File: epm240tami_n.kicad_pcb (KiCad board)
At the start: 2 copper layers, 63.5 x 41.9 mm, 25 parts, among them CON1 BARREL_JACK, P1 CONN_01X03, P2 CONN_01X02, P3 CONN_01X03, P4 CONN_02X22, P5 CONN_02X22, P6 JTAG, P7 CONN_01X07, U1 EPM240T100C5N, U2 NCP1117ST33T3G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

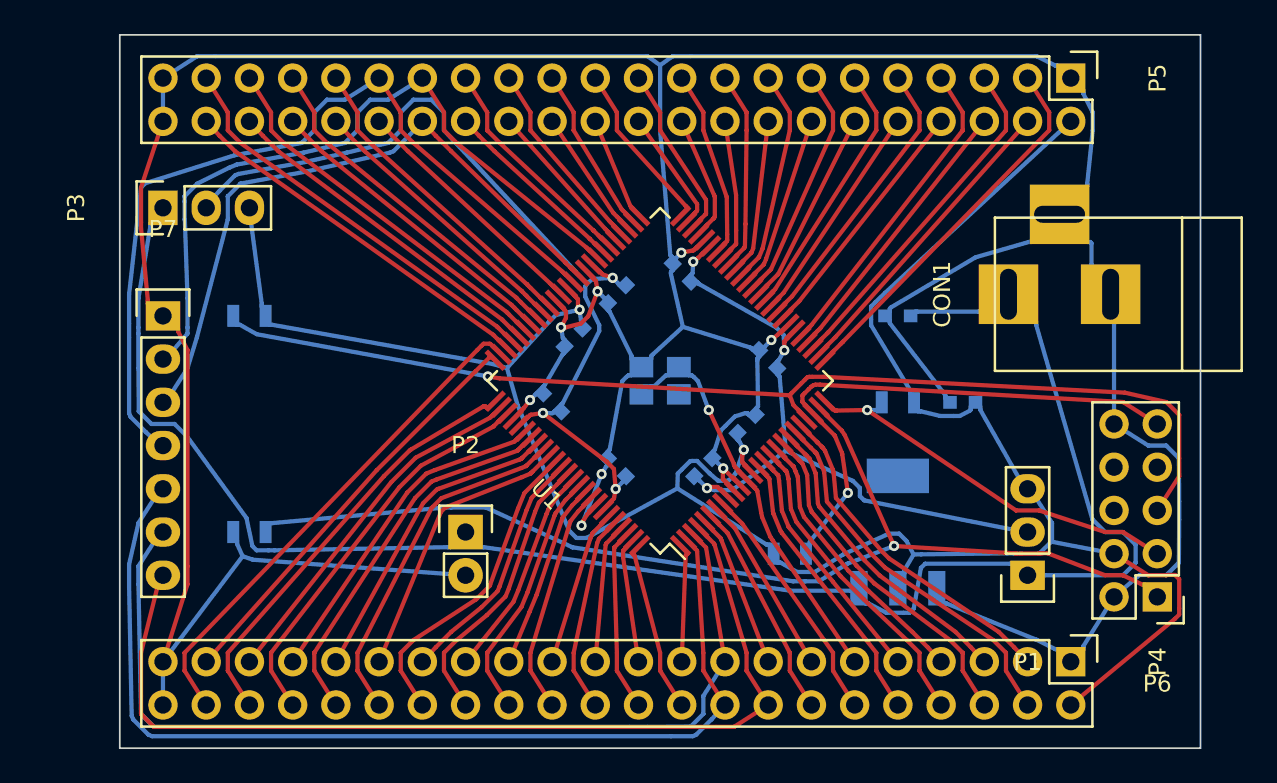
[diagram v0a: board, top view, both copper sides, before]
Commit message: Updated schematic and moved DI/DO around to reduce routing due to new placement. Added PDF file
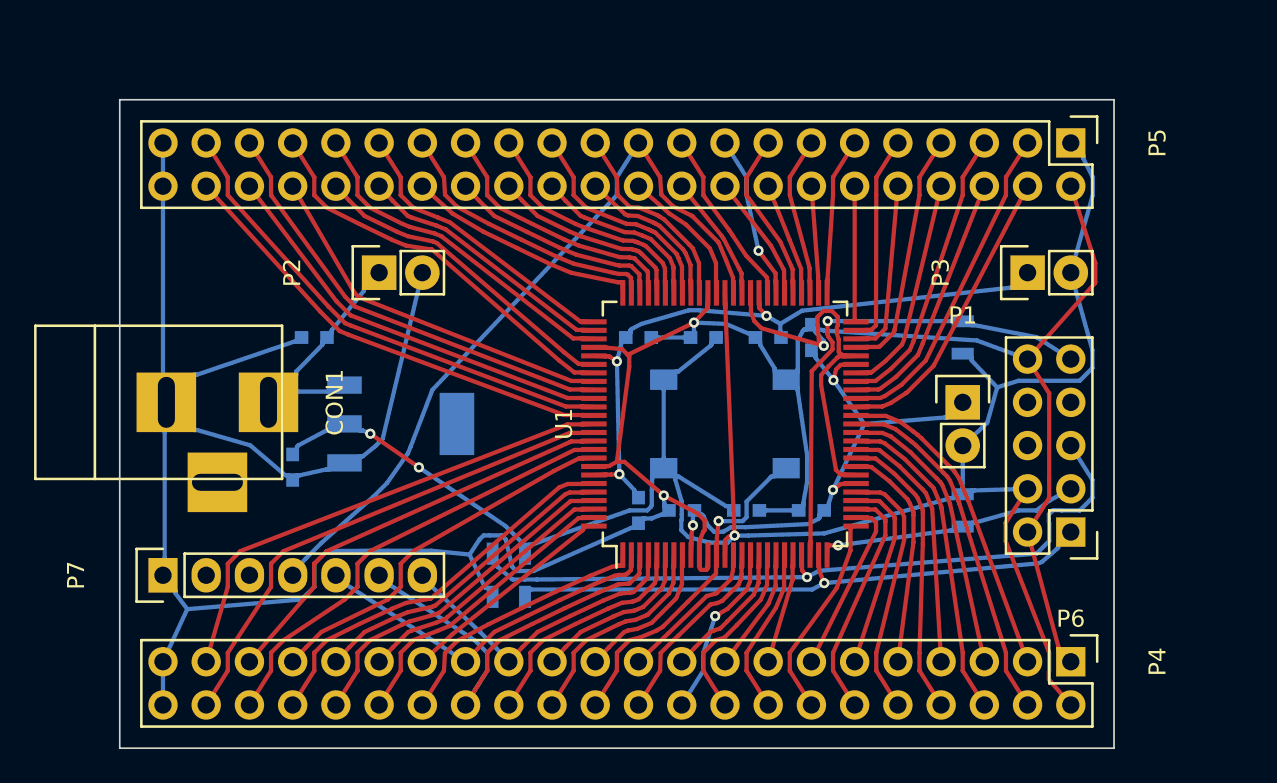
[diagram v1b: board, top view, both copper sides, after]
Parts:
- CON1: value BARREL_JACK -> AB2_POWER_BARREL
- P1, P3: value CONN_01X03 -> CONN_01X02; footprint Pin_Headers:Pin_Header_Straight_1x03 -> Pin_Headers:Pin_Header_Straight_1x02
- U2: value NCP1117ST33T3G -> AMS1117-3.3V
- X1: footprint Crystals_Oscillators_SMD:crystal_FA238-TSX3225 -> Crystals_Oscillators_SMD:crystal_HXO-3
- moved CON1 56.2 mm to (128.3, 63.5), turned to 0 degrees
- moved P3 50.9 mm to (179.1, 55.9)
- moved C2 39.6 mm to (135.9, 67.3), turned to 270 degrees
- moved C1 34.3 mm to (137.2, 59.7)
- moved U2 29.9 mm to (142.2, 64.8), turned to 90 degrees
- moved R3 20.7 mm to (148.6, 72.4)
- moved R2 16.3 mm to (175.3, 59.7), turned to 90 degrees
- moved P2 16.1 mm to (141.0, 55.9), turned to 90 degrees
- moved C7 15.9 mm to (166.4, 69.8), turned to 180 degrees
- moved R1 15.7 mm to (148.6, 74.9)
- moved P7 15.2 mm to (128.3, 73.7), turned to 90 degrees
- moved P1 10.9 mm to (175.3, 63.5), turned to 0 degrees
- moved C9 9.25 mm to (163.8, 59.7), turned to 180 degrees
- moved C4 7.62 mm to (160.0, 59.7), turned to 180 degrees
- moved R4 7.41 mm to (175.3, 69.8), turned to 270 degrees
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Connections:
- CON1 pad 3: GND -> (no net)
- P1 pad 1: VCC -> /VCCIO1
- P1 pad 2: /VCCIO1 -> +3V3
- P3 pad 1: VCC -> /VCCIO2
- P3 pad 2: /VCCIO2 -> +3V3
- P4 pad 10: /IO14 -> /IO30
- P4 pad 11: /CLK_CORE -> /IO29
- P4 pad 12: /IO8 -> /IO28
- P4 pad 13: /IO7 -> /IO27
- P4 pad 14: /IO6 -> /IO26
- P4 pad 15: /IO5 -> /IO21
- P4 pad 16: /DP2 -> /IO20
- P4 pad 17: /DP1 -> /IO19
- P4 pad 18: /DM -> /IO18
- P4 pad 19: /IO1 -> /IO17
- P4 pad 20: /IO100 -> /IO16
- P4 pad 21: /IO99 -> /IO14
- P4 pad 22: /IO98 -> /IO15
- P4 pad 23: /IO97 -> /IO8
- P4 pad 24: /IO96 -> /CLK_CORE
- P4 pad 25: /IO95 -> /IO6
- P4 pad 26: /IO92 -> /IO7
- P4 pad 27: /IO91 -> /DP2
- P4 pad 28: /IO90 -> /IO5
- P4 pad 29: /IO89 -> /DM
- P4 pad 3: /IO21 -> /IO39
- P4 pad 30: /IO88 -> /DP1
- P4 pad 31: /IO87 -> /IO100
- P4 pad 32: /IO86 -> /IO1
- P4 pad 33: /IO85 -> /IO98
- P4 pad 34: /IO84 -> /IO99
- P4 pad 35: /IO83 -> /IO96
- P4 pad 36: /IO82 -> /IO97
- P4 pad 37: /IO81 -> /IO92
- P4 pad 38: /IO78 -> /IO95
- P4 pad 39: /IO77 -> /IO90
- P4 pad 4: /IO20 -> /IO38
- P4 pad 40: /IO76 -> /IO91
- P4 pad 41: /IO75 -> /DI
- P4 pad 42: /IO74 -> /DO
- P4 pad 5: /IO19 -> /IO37
- P4 pad 6: /IO18 -> /IO36
- P4 pad 7: /IO17 -> /IO35
- P4 pad 8: /IO16 -> /IO34
- P4 pad 9: /IO15 -> /IO33
- P5 pad 1: GND -> +3V3
- P5 pad 10: /IO35 -> /IO48
- P5 pad 11: /IO36 -> /IO51
- P5 pad 12: /IO37 -> /IO50
- P5 pad 13: /IO38 -> /IO53
- P5 pad 14: /IO39 -> /IO52
- P5 pad 15: /IO40 -> /IO55
- P5 pad 16: /IO41 -> /IO54
- P5 pad 17: /IO42 -> /IO57
- P5 pad 18: /IO43 -> /IO56
- P5 pad 19: /IO44 -> /IO58
- P5 pad 2: +3V3 -> GND
- P5 pad 20: /IO47 -> /IO61
- P5 pad 21: /IO48 -> /IO62
- P5 pad 22: /IO49 -> /IO64
- P5 pad 23: /IO50 -> /IO66
- P5 pad 24: /IO51 -> /IO67
- P5 pad 25: /IO52 -> /IO68
- P5 pad 26: /IO53 -> /IO69
- P5 pad 27: /IO54 -> /IO70
- P5 pad 28: /IO55 -> /IO71
- P5 pad 29: /IO56 -> /IO72
- P5 pad 3: /IO26 -> /IO41
- P5 pad 30: /IO57 -> /IO73
- P5 pad 31: /DI -> /IO74
- P5 pad 32: /DO -> /IO75
- P5 pad 33: /IO62 -> /IO76
- P5 pad 34: /IO64 -> /IO77
- P5 pad 35: /IO66 -> /IO78
- P5 pad 36: /IO67 -> /IO81
- P5 pad 37: /IO68 -> /IO82
- P5 pad 38: /IO69 -> /IO83
- P5 pad 39: /IO70 -> /IO84
- P5 pad 4: /IO27 -> /IO40
- P5 pad 40: /IO71 -> /IO85
- P5 pad 41: /IO72 -> /IO86
- P5 pad 42: /IO73 -> /IO87
- P5 pad 5: /IO28 -> /IO43
- P5 pad 6: /IO29 -> /IO42
- P5 pad 7: /IO30 -> /IO47
- P5 pad 8: /IO33 -> /IO44
- P5 pad 9: /IO34 -> /IO49
- U1 pad 58: /DI -> /IO58
- U1 pad 61: /DO -> /IO61
- U1 pad 88: /IO88 -> /DI
- U1 pad 89: /IO89 -> /DO
- X1 pad 1: (no net) -> +3V3
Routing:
- net VCC: track 104.5 -> 14.9 mm
- net /DP2: track 57.4 -> 18.3 mm
- net /DM: track 60.4 -> 21.4 mm
- net GND: track 257.1 -> 224.3 mm, vias 8 -> 3
- net /DP1: track 56.3 -> 26.1 mm
- net /TCK: track 64.0 -> 35.0 mm
- net /TMS: track 64.9 -> 43.3 mm
- net /IO88: track 16.6 -> 0.00 mm
- net /IO91: track 11.1 -> 26.8 mm
- net /VCCIO2: track 54.5 -> 40.2 mm
- net /IO95: track 9.36 -> 23.2 mm
- net /IO74: track 30.0 -> 16.4 mm
- net /IO21: track 19.9 -> 6.48 mm
- net /IO87: track 14.4 -> 27.4 mm
- net /DI: track 42.1 -> 29.3 mm
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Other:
- board size 63.5 x 41.9 mm -> 58.4 x 38.1 mm
